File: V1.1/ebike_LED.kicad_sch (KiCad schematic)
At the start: 5 parts, among them SW1 SW_Push

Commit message: gerber generation
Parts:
- added R2: 10k, Resistor_SMD:R_0805_2012Metric, symbol Device:R
- added SW2: SW_Push, Button_Switch_THT:SW_PUSH-12mm, symbol Switch:SW_Push
- SW1: footprint Button_Switch_THT:SW_PUSH_6mm_H8mm -> Button_Switch_THT:SW_PUSH-12mm
- renumbered R6 to R1
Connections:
- net +3.3v: now also LED1.2 (Pin_2), R2.1; no longer LED1.1 (Pin_1)
- net GND: now also SW2.2
- net Vcc: now also LED1.1 (Pin_1); no longer LED1.2 (Pin_2)
- net PB2_IN: now reaches A1.25 (A12/IO13)
- net PB2_IN: now also R2.2, SW2.1
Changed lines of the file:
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@@
 (kicad_sch (version 20211123) (generator eeschema)
   (paper "User" 228.6 152.4)
+  (junction (at 108.458 83.82) (diameter 0) (color 0 0 0 0)
+  )
   (junction (at 108.458 66.04) (diameter 0) (color 0 0 0 0)
   )
+  (wire (pts (xy 121.285 36.83) (xy 121.285 34.798))
+    (stroke (width 0) (type default) (color 0 0 0 0))
+  )
   (wire (pts (xy 120.65 66.04) (xy 123.19 66.04))
     (stroke (width 0) (type default) (color 0 0 0 0))
   )
+  (wire (pts (xy 108.458 72.898) (xy 108.458 71.755))
+    (stroke (width 0) (type default) (color 0 0 0 0))
+  )
+  (wire (pts (xy 54.864 49.784) (xy 57.531 49.784))
+    (stroke (width 0) (type default) (color 0 0 0 0))
+  )
   (wire (pts (xy 123.825 36.83) (xy 123.825 34.798))
     (stroke (width 0) (type default) (color 0 0 0 0))
@@
     (stroke (width 0) (type default) (color 0 0 0 0))
   )
-  (wire (pts (xy 121.285 36.83) (xy 121.285 34.798))
-    (stroke (width 0) (type default) (color 0 0 0 0))
-  )
-  (wire (pts (xy 127.889 23.114) (xy 125.984 23.114))
-    (stroke (width 0) (type default) (color 0 0 0 0))
-  )
-  (wire (pts (xy 125.984 19.939) (xy 127.889 19.939))
+  (wire (pts (xy 108.458 83.82) (xy 110.49 83.82))
     (stroke (width 0) (type default) (color 0 0 0 0))
   )
@@
     (stroke (width 0) (type default) (color 0 0 0 0))
   )
-  (wire (pts (xy 127.889 19.939) (xy 127.889 23.114))
-    (stroke (width 0) (type default) (color 0 0 0 0))
-  )
   (wire (pts (xy 54.991 67.564) (xy 57.531 67.564))
     (stroke (width 0) (type default) (color 0 0 0 0))
@@
     (stroke (width 0) (type default) (color 0 0 0 0))
   )
+  (wire (pts (xy 106.68 83.82) (xy 108.458 83.82))
+    (stroke (width 0) (type default) (color 0 0 0 0))
+  )
   (wire (pts (xy 126.365 36.83) (xy 126.365 34.798))
     (stroke (width 0) (type default) (color 0 0 0 0))
   )
+  (wire (pts (xy 120.65 83.82) (xy 123.19 83.82))
+    (stroke (width 0) (type default) (color 0 0 0 0))
+  )
   (wire (pts (xy 54.991 47.244) (xy 57.531 47.244))
     (stroke (width 0) (type default) (color 0 0 0 0))
@@
     (stroke (width 0) (type default) (color 0 0 0 0))
   )
+  (wire (pts (xy 108.458 71.755) (xy 107.188 71.755))
+    (stroke (width 0) (type default) (color 0 0 0 0))
+  )
   (wire (pts (xy 108.458 55.118) (xy 108.458 53.975))
     (stroke (width 0) (type default) (color 0 0 0 0))
@@
     (stroke (width 0) (type default) (color 0 0 0 0))
   )
+  (wire (pts (xy 108.458 80.518) (xy 108.458 83.82))
+    (stroke (width 0) (type default) (color 0 0 0 0))
+  )
   (wire (pts (xy 96.52 36.83) (xy 96.52 34.798))
     (stroke (width 0) (type default) (color 0 0 0 0))
@@
     (effects (font (size 1.27 1.27)) (justify right))
     (property "Intersheet References" "${INTERSHEET_REFS}" (id 0) (at -19.431 -7.62 0)
-      (effects (font (size 1.27 1.27)) hide)
-    )
-  )
-  (global_label "Vi2c" (shape input) (at 121.285 36.83 270) (fields_autoplaced)
-    (effects (font (size 1.27 1.27)) (justify right))
-    (property "Intersheet References" "${INTERSHEET_REFS}" (id 0) (at -19.431 -7.62 0)
-      (effects (font (size 1.27 1.27)) hide)
-    )
-  )
-  (global_label "+3.3v" (shape input) (at 125.984 19.939 180) (fields_autoplaced)
-    (effects (font (size 1.27 1.27)) (justify right))
-    (property "Intersheet References" "${INTERSHEET_REFS}" (id 0) (at -24.511 -37.211 0)
       (effects (font (size 1.27 1.27)) hide)
     )
@@
     )
   )
+  (global_label "PB2_IN" (shape input) (at 106.68 83.82 180) (fields_autoplaced)
+    (effects (font (size 1.27 1.27)) (justify right))
+    (property "Intersheet References" "${INTERSHEET_REFS}" (id 0) (at 97.7034 83.7406 0)
+      (effects (font (size 1.27 1.27)) (justify right) hide)
+    )
+  )
+  (global_label "GND" (shape input) (at 123.19 83.82 0) (fields_autoplaced)
+    (effects (font (size 1.27 1.27)) (justify left))
+    (property "Intersheet References" "${INTERSHEET_REFS}" (id 0) (at -10.795 12.446 0)
+      (effects (font (size 1.27 1.27)) hide)
+    )
+  )
   (global_label "GND" (shape input) (at 123.19 66.04 0) (fields_autoplaced)
     (effects (font (size 1.27 1.27)) (justify left))
@@
     )
   )
+  (global_label "Vcc" (shape input) (at 121.285 36.83 270) (fields_autoplaced)
+    (effects (font (size 1.27 1.27)) (justify right))
+    (property "Intersheet References" "${INTERSHEET_REFS}" (id 0) (at 5.334 -7.62 0)
+      (effects (font (size 1.27 1.27)) hide)
+    )
+  )
   (global_label "RX" (shape input) (at 99.06 36.83 270) (fields_autoplaced)
     (effects (font (size 1.27 1.27)) (justify right))
@@
     )
   )
+  (global_label "+3.3v" (shape input) (at 107.188 71.755 180) (fields_autoplaced)
+    (effects (font (size 1.27 1.27)) (justify right))
+    (property "Intersheet References" "${INTERSHEET_REFS}" (id 0) (at -12.954 10.668 0)
+      (effects (font (size 1.27 1.27)) hide)
+    )
+  )
   (global_label "TX" (shape input) (at 101.6 36.83 270) (fields_autoplaced)
     (effects (font (size 1.27 1.27)) (justify right))
@@
     )
   )
-  (global_label "Vi2c" (shape input) (at 125.984 23.114 180) (fields_autoplaced)
-    (effects (font (size 1.27 1.27)) (justify right))
-    (property "Intersheet References" "${INTERSHEET_REFS}" (id 0) (at -24.511 -37.211 0)
-      (effects (font (size 1.27 1.27)) hide)
+  (global_label "PB2_IN" (shape input) (at 54.864 49.784 180) (fields_autoplaced)
+    (effects (font (size 1.27 1.27)) (justify right))
+    (property "Intersheet References" "${INTERSHEET_REFS}" (id 0) (at 45.8874 49.7046 0)
+      (effects (font (size 1.27 1.27)) (justify right) hide)
     )
   )
@@
     )
   )
-  (global_label "Vcc" (shape input) (at 123.825 36.83 270) (fields_autoplaced)
-    (effects (font (size 1.27 1.27)) (justify right))
-    (property "Intersheet References" "${INTERSHEET_REFS}" (id 0) (at -19.431 -7.62 0)
-      (effects (font (size 1.27 1.27)) hide)
+  (global_label "+3.3v" (shape input) (at 123.825 36.83 270) (fields_autoplaced)
+    (effects (font (size 1.27 1.27)) (justify right))
+    (property "Intersheet References" "${INTERSHEET_REFS}" (id 0) (at 123.7456 44.718 90)
+      (effects (font (size 1.27 1.27)) (justify right) hide)
     )
   )
@@
   (symbol (lib_id "Device:R") (at 108.458 58.928 0) (unit 1)
     (in_bom yes) (on_board yes)
-    (property "Reference" "R6" (id 0) (at 104.648 57.785 0)
+    (property "Reference" "R1" (id 0) (at 104.648 57.785 0)
       (effects (font (size 1.27 1.27)) (justify left))
     )
@@
     (property "Reference" "SW1" (id 0) (at 115.57 58.42 0))
     (property "Value" "SW_Push" (id 1) (at 115.57 60.96 0))
-    (property "Footprint" "Button_Switch_THT:SW_PUSH_6mm_H8mm" (id 2) (at 115.57 60.96 0)
+    (property "Footprint" "Button_Switch_THT:SW_PUSH-12mm" (id 2) (at 115.57 60.96 0)
       (effects (font (size 1.27 1.27)) hide)
     )
@@
     (pin "9")
   )
+  (symbol (lib_id "Device:R") (at 108.458 76.708 0) (unit 1)
+    (in_bom yes) (on_board yes)
+    (property "Reference" "R2" (id 0) (at 104.648 75.565 0)
+      (effects (font (size 1.27 1.27)) (justify left))
+    )
+    (property "Value" "10k" (id 1) (at 103.759 77.978 0)
+      (effects (font (size 1.27 1.27)) (justify left))
+    )
+    (property "Footprint" "Resistor_SMD:R_0805_2012Metric" (id 2) (at 106.68 76.708 90)
+      (effects (font (size 1.27 1.27)) hide)
+    )
+    (property "Datasheet" "https://www.mouser.com/ProductDetail/ROHM-Semiconductor/ESR10EZPF5102?qs=DyUWGjl%252BcVsMTSBF51O24w%3D%3D" (id 3) (at 108.458 76.708 0)
+      (effects (font (size 1.27 1.27)) hide)
+    )
+    (property "P/N" "755-ESR10EZPF5102" (id 4) (at 108.458 76.708 0)
+      (effects (font (size 1.27 1.27)) hide)
+    )
+    (property "Group#" "11" (id 5) (at 108.458 76.708 0)
+      (effects (font (size 1.27 1.27)) hide)
+    )
+    (pin "1")
+    (pin "2")
+  )
+  (symbol (lib_id "Switch:SW_Push") (at 115.57 83.82 0) (unit 1)
+    (in_bom yes) (on_board yes) (fields_autoplaced)
+    (property "Reference" "SW2" (id 0) (at 115.57 76.2 0))
+    (property "Value" "SW_Push" (id 1) (at 115.57 78.74 0))
+    (property "Footprint" "Button_Switch_THT:SW_PUSH-12mm" (id 2) (at 115.57 78.74 0)
+      (effects (font (size 1.27 1.27)) hide)
+    )
+    (property "Datasheet" "~" (id 3) (at 115.57 78.74 0)
+      (effects (font (size 1.27 1.27)) hide)
+    )
+    (pin "1")
+    (pin "2")
+  )
   (sheet_instances
     (path "/" (page "1"))
@@
     )
     (path "/00000000-0000-0000-0000-00005e6163c4"
-      (reference "R6") (unit 1) (value "10k") (footprint "Resistor_SMD:R_0805_2012Metric")
+      (reference "R1") (unit 1) (value "10k") (footprint "Resistor_SMD:R_0805_2012Metric")
+    )
+    (path "/c2cf7261-51ef-4f85-9c06-599b53883481"
+      (reference "R2") (unit 1) (value "10k") (footprint "Resistor_SMD:R_0805_2012Metric")
     )
     (path "/00000000-0000-0000-0000-00005e6b7bfe"
@@
     )
     (path "/62d92c20-0867-45d7-93fc-db1146a4ad7d"
-      (reference "SW1") (unit 1) (value "SW_Push") (footprint "Button_Switch_THT:SW_PUSH_6mm_H8mm")
-    )
-  )
+      (reference "SW1") (unit 1) (value "SW_Push") (footprint "Button_Switch_THT:SW_PUSH-12mm")
+    )
+    (path "/f6db14fb-4f29-463a-a806-6eb74b6f13d0"
+      (reference "SW2") (unit 1) (value "SW_Push") (footprint "Button_Switch_THT:SW_PUSH-12mm")
+    )
+  )

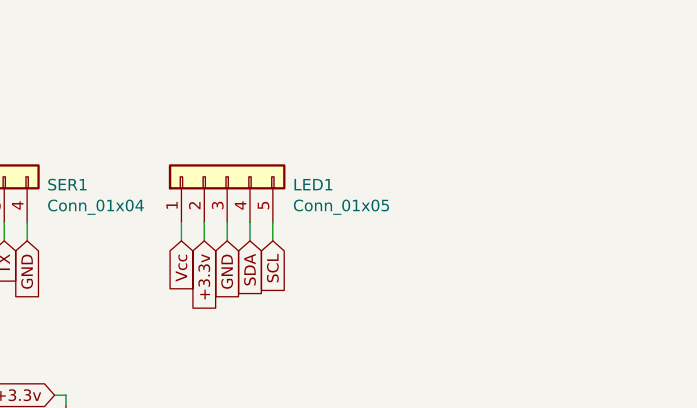
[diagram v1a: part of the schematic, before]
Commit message: fixed timer reset
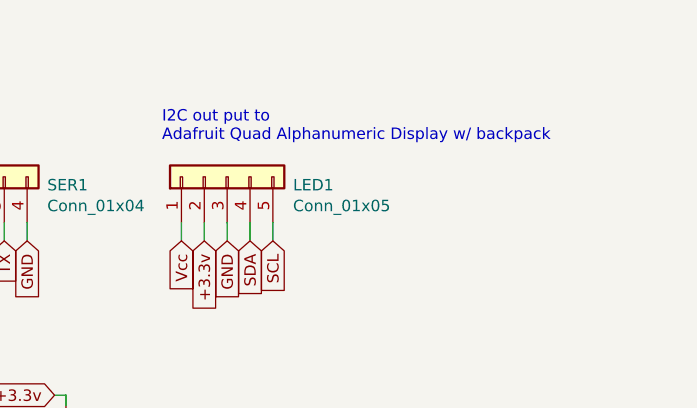
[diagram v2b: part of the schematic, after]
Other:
- note added: "I2C out put to Adafruit Quad Alphanumeric Display w/ backpack"
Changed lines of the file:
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@@
     (stroke (width 0) (type default) (color 0 0 0 0))
+  )
+  (text "I2C out put to\nAdafruit Quad Alphanumeric Display w/ backpack"
+    (at 119.126 25.908 0)
+    (effects (font (size 1.27 1.27)) (justify left bottom))
   )
   (global_label "Vcc" (shape input) (at 96.52 36.83 270) (fields_autoplaced)
